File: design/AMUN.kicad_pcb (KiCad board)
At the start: 2 copper layers, 60 x 40 mm, 52 parts, among them IC2 SHT40-AD1B-R2, IC3 SGP40-D-R4, IC4 AZ1117CH-3.3TRG1, IC5 STM32L431CCT6TR, J1 UJ20-C-H-G-MSMT-4B-P16-TR, J2 Conn_ARM_SWD_TagConnect_TC203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, J3 Conn_01x02_Pin, J4 Conn_01x02_Pin, J5 Conn_01x02_Pin, J6 SFV12R-1STBE1HLF, Q2 SSM3K16FV,L3F, U2 ER-TFT018-3

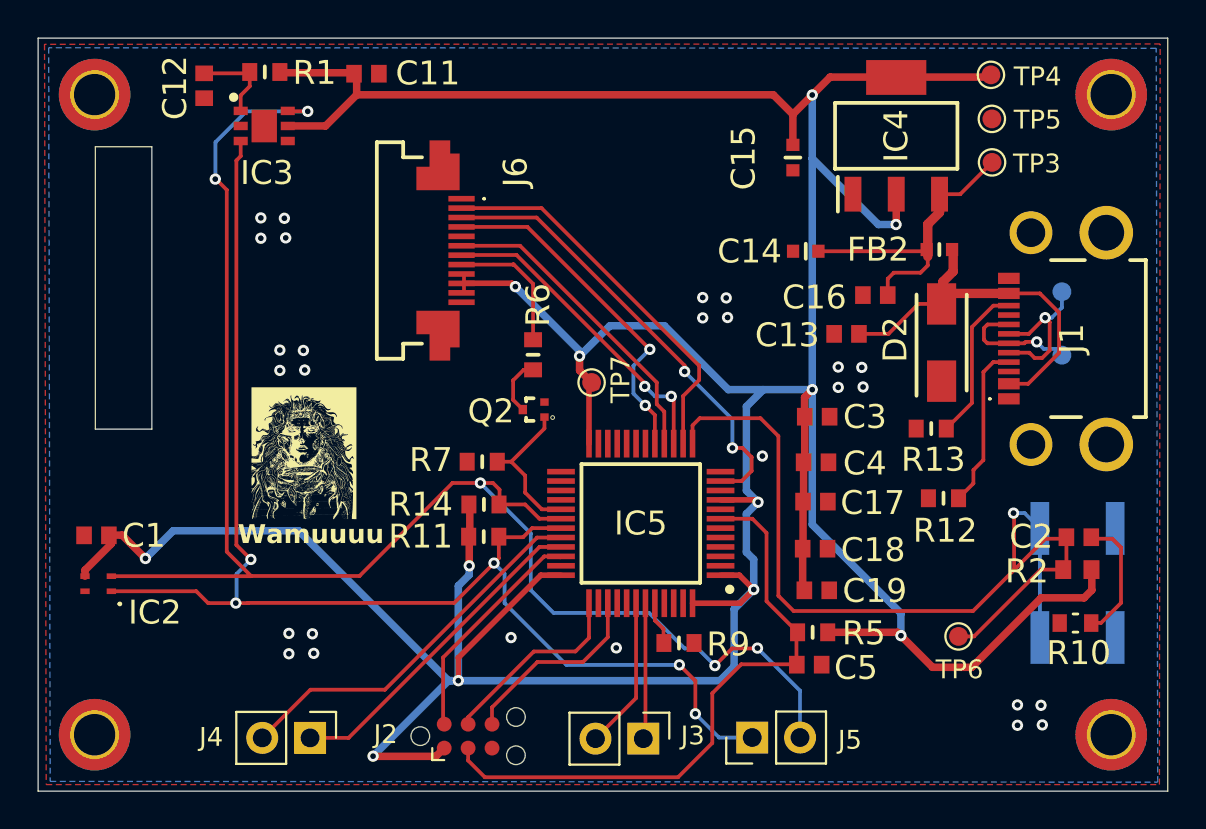
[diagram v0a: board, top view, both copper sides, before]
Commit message: - Added display.kicad_sch; - Added mounting holes on schematic; - Removed TAG connect pads and used pin header; - Cut the PCB in order to make space for USB connector; - Changed mounting holes foorprint to non-plated ones; - Cut board near SHT4x sensor in order to reduce heat contribution from the rest of the board; - Re-routing; - Added revision number on silkscreen; - Shrunk components ID on silkscreen.
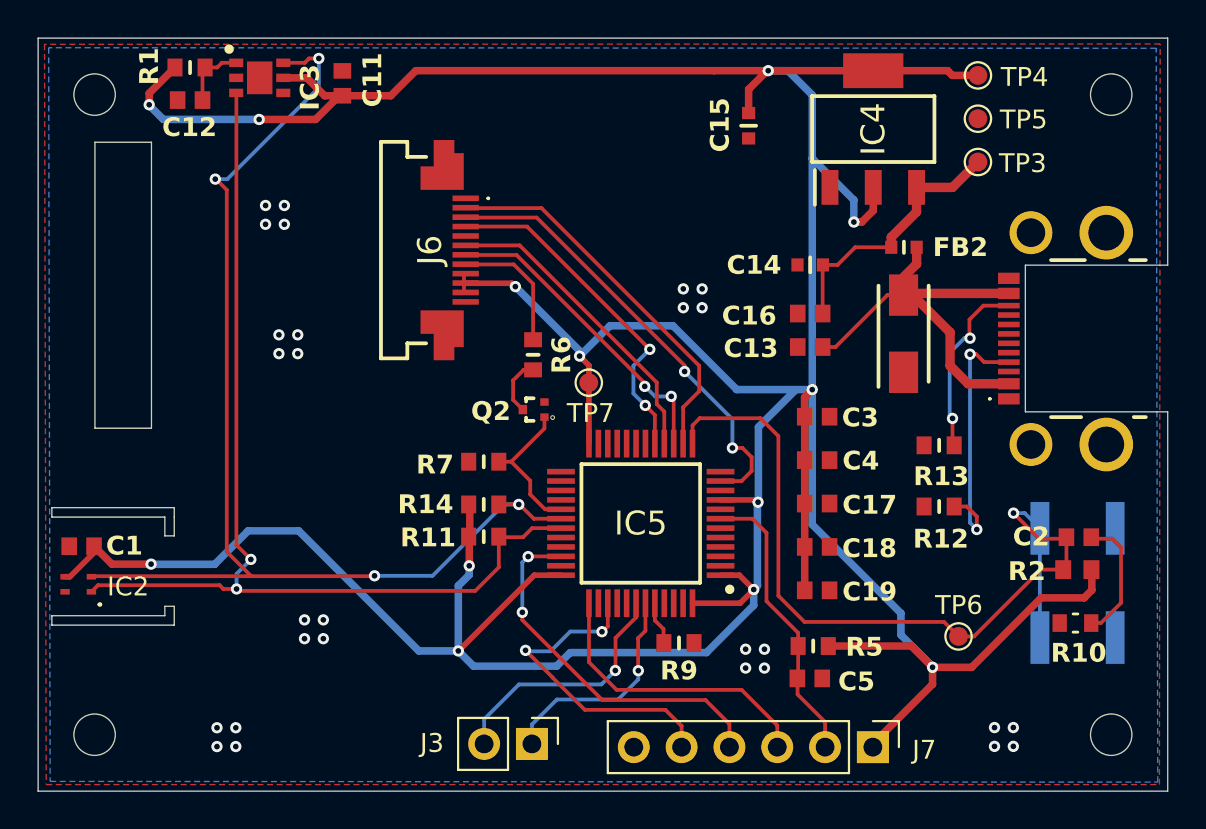
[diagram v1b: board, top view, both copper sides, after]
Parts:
- removed G***: LOGO, amun_lib:cursed
- removed J2: Conn_ARM_SWD_TagConnect_TC2030-NL, Connector:Tag-Connect_TC2030-IDC-NL_2x03_P1.27mm_Vertical
- removed J4, J5: Conn_01x02_Pin, Connector_PinHeader_2.54mm:PinHeader_1x02_P2.54mm_Vertical
- removed REF** (x4): MountingHole_2.2mm_M2_DIN965_Pad_TopBottom, MountingHole:MountingHole_2.2mm_M2_DIN965_Pad_TopBottom
- removed TP1: DP, TestPoint:TestPoint_Pad_D1.0mm
- removed TP2: DN, TestPoint:TestPoint_Pad_D1.0mm
- added H1: MountingHole, MountingHole:MountingHole_2.2mm_M2_DIN965, F.Cu at (148.1, 54.0)
- added H2: MountingHole, MountingHole:MountingHole_2.2mm_M2_DIN965, F.Cu at (148.1, 88.0)
- added H3: MountingHole, MountingHole:MountingHole_2.2mm_M2_DIN965, F.Cu at (94.0, 88.0)
- added H4: MountingHole, MountingHole:MountingHole_2.2mm_M2_DIN965, F.Cu at (94.0, 54.0)
- added J7: Conn_01x06, Connector_PinHeader_2.54mm:PinHeader_1x06_P2.54mm_Vertical, F.Cu at (135.4, 88.7)
- moved J3 5.92 mm to (117.3, 88.5)
- moved R1 3.98 mm to (99.1, 52.6), turned to 180 degrees
- moved C16 3.60 mm to (132.1, 65.7)
- moved C15 2.89 mm to (128.8, 55.7)
- moved IC3 2.57 mm to (102.8, 53.1)
- moved D2 2.07 mm to (137.0, 66.7)
- moved C13 2.05 mm to (132.1, 67.4)
- moved FB2 1.88 mm to (137.0, 62.1)
- moved C11 1.38 mm to (107.2, 53.4), turned to 90 degrees
- moved IC4 1.27 mm to (135.4, 55.9)
- moved C12 1.07 mm to (99.1, 54.3), turned to 180 degrees
- moved IC2 1.06 mm to (93.2, 80.0)
- moved R13 0.98 mm to (138.9, 72.7)
- moved C1 0.98 mm to (93.4, 78.0)
- moved C14 0.76 mm to (132.1, 63.1)
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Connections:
- net Net-(J6-Pad8) renamed /Display/LEDK
- J1 pad A6: Net-(J1-DP1) -> unconnected-(J1-DP1-PadA6)
- J1 pad A7: Net-(J1-DN1) -> unconnected-(J1-DN1-PadA7)
- J1 pad B6: Net-(J1-DP1) -> unconnected-(J1-DP2-PadB6)
- J1 pad B7: Net-(J1-DN1) -> unconnected-(J1-DN2-PadB7)
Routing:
- net /I2C_SCL: track 84.1 -> 60.8 mm, vias 5 -> 4
- net /MCU/MCU_IO_11: track 20.3 -> 0.00 mm
- net /MCU/MCU_NRST: track 32.9 -> 15.3 mm
- net /MCU/MCU_IO_12: track 17.5 -> 0.00 mm
- net /I2C_SDA: track 71.1 -> 54.5 mm, vias 5 -> 2
- net Net-(J1-DN1): track 8.53 -> 0.00 mm, vias 1 -> 0
- net /MCU/MCU_SWDIO: track 12.1 -> 19.8 mm, vias 0 -> 2
- net /MCU/MCU_SWO: track 10.4 -> 17.3 mm, vias 0 -> 2
- net Net-(J1-DP1): track 6.57 -> 0.00 mm, vias 1 -> 0
- net /MCU/BUTTON: track 51.4 -> 45.0 mm
- net /MCU/USART_TX_DEVELOP: track 8.09 -> 13.4 mm, vias 0 -> 1
- net /MCU/MCU_SWCLK: track 10.4 -> 15.5 mm
- net Net-(J1-CC1): track 8.82 -> 13.8 mm, vias 0 -> 2
- net /MCU/USART_RX_DEVELOP: track 7.98 -> 11.9 mm, vias 0 -> 1
- net +3V3: track 234.3 -> 237.8 mm, vias 12 -> 13
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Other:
- outline, holes or cut-outs redrawn
- board text added: "Rev: 1.1"
- board text removed: "Wamuuuu"

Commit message: Updated 3D models of components; Addend new PCB renders; Updated README.md; Updated board to revision 2.0; Schematic and layout cleanup and minor changes.
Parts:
- renumbered TP4 to 3V3, TP7 to 3V3, TP3 to 5V, TP6 to BTN, TP5 to GND
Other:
- board text added: "Rev: 2.0"
- board text removed: "Rev: 1.1"
